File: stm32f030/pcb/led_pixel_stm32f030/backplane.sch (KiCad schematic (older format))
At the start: 3 parts, among them J1 Screw_Terminal_1x02, J2 CONN_01X10, J3 CONN_01X10

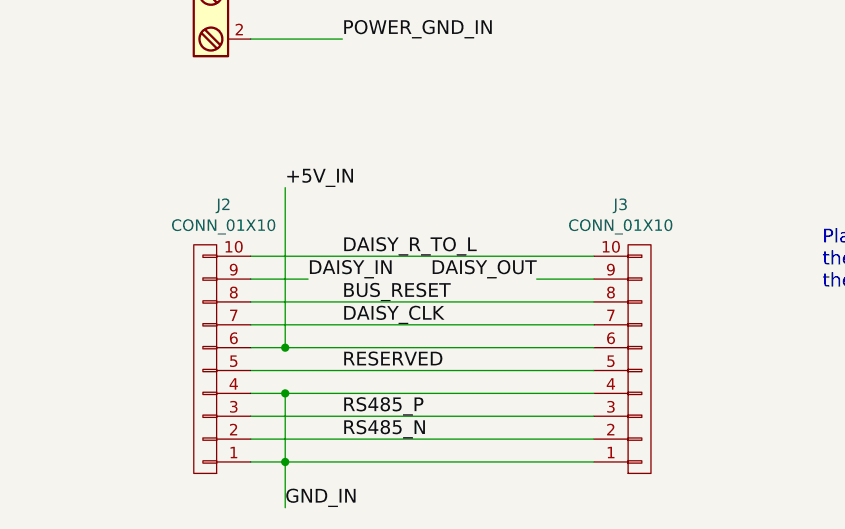
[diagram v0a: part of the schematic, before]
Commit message: made a first layout draft...
well okay, wouldn´t call it layout yet ;)

- next step make it look like a Layout XD
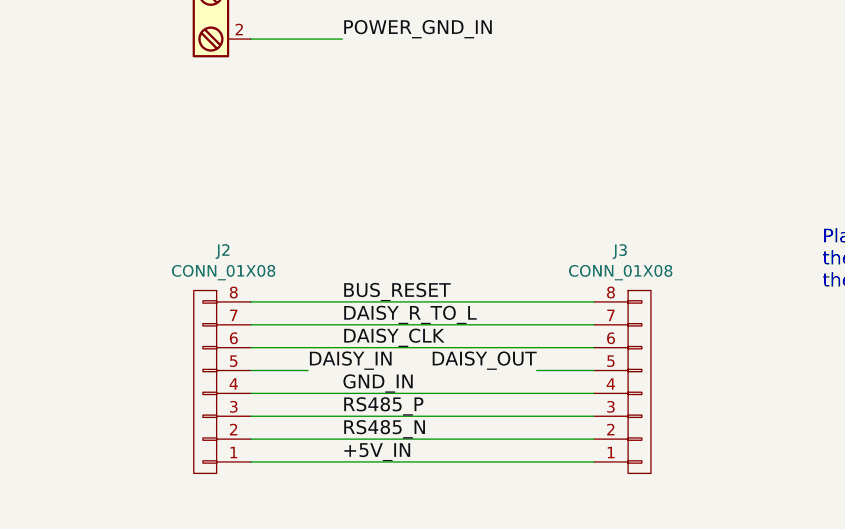
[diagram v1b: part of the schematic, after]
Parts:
- removed J2, J3: CONN_01X10, Pin_Headers:Pin_Header_Straight_1x10_Pitch2.54mm, symbol CONN_01X10
- added J2, J3: CONN_01X08, Pin_Headers:Pin_Header_Straight_1x08_Pitch2.54mm, symbol CONN_01X08
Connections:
- net +5V_IN: now also J2.1 (P1), J3.1 (P1)
- net BUS_RESET: now also J2.8 (P8), J3.8 (P8)
- net DAISY_CLK: now also J2.6 (P6), J3.6 (P6)
- net DAISY_IN: now also J2.5 (P5)
- net DAISY_OUT: now also J3.5 (P5)
- net DAISY_R_TO_L: now also J2.7 (P7), J3.7 (P7)
- net GND_IN: now also J2.4 (P4), J3.4 (P4)
- net RS485_N: now also J2.2 (P2), J3.2 (P2)
- net RS485_P: now also J2.3 (P3), J3.3 (P3)
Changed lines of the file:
@@
 $EndDescr
-$Comp
-L CONN_01X10 J2
-U 1 1 5905FA3B
-P 3400 3350
-F 0 "J2" H 3319 2675 50  0000 C CNN
-F 1 "CONN_01X10" H 3319 2766 50  0000 C CNN
-F 2 "Pin_Headers:Pin_Header_Straight_1x10_Pitch2.54mm" H 3400 3350 50  0001 C CNN
-F 3 "" H 3400 3350 50  0001 C CNN
-	1    3400 3350
-	-1   0    0    1
-$EndComp
-$Comp
-L CONN_01X10 J3
-U 1 1 5905FABB
-P 5300 3350
-F 0 "J3" H 5218 2675 50  0000 C CNN
-F 1 "CONN_01X10" H 5218 2766 50  0000 C CNN
-F 2 "Pin_Headers:Pin_Header_Straight_1x10_Pitch2.54mm" H 5300 3350 50  0001 C CNN
-F 3 "" H 5300 3350 50  0001 C CNN
-	1    5300 3350
-	1    0    0    1
-$EndComp
 $Comp
 L Screw_Terminal_1x02 J1
@@
 	1    0    0    -1
 $EndComp
-Wire Wire Line
-	3600 1750 4000 1750
-Wire Wire Line
-	3600 1950 4000 1950
-Wire Wire Line
-	3600 2900 5100 2900
-Wire Wire Line
-	3600 3500 5100 3500
-Wire Wire Line
-	3600 3800 5100 3800
-Wire Wire Line
-	3600 3700 5100 3700
-Wire Wire Line
-	5100 3600 3600 3600
-Wire Wire Line
-	3750 3500 3750 4000
-Connection ~ 3750 3800
-Connection ~ 3750 3500
 Text Label 4000 3600 0    60   ~ 0
 RS485_P
 Text Label 4000 3700 0    60   ~ 0
 RS485_N
-Text Label 4000 2900 0    60   ~ 0
+Text Label 4000 3200 0    60   ~ 0
 DAISY_R_TO_L
-Text Label 3850 3000 0    60   ~ 0
+Text Label 3850 3400 0    60   ~ 0
 DAISY_IN
-Text Label 4850 3000 2    60   ~ 0
+Text Label 4850 3400 2    60   ~ 0
 DAISY_OUT
-Wire Wire Line
-	5100 3000 4850 3000
-Wire Wire Line
-	3850 3000 3600 3000
-Wire Wire Line
-	5100 3100 3600 3100
 Text Label 4000 3100 0    60   ~ 0
 BUS_RESET
-Text Label 4000 3200 0    60   ~ 0
+Text Label 4000 3300 0    60   ~ 0
 DAISY_CLK
-Wire Wire Line
-	3600 3200 5100 3200
-Wire Wire Line
-	3600 3300 5100 3300
-Wire Wire Line
-	5100 3400 3600 3400
-Wire Wire Line
-	3750 2600 3750 3300
-Connection ~ 3750 3300
-Text Label 4000 3400 0    60   ~ 0
-RESERVED
 Text Notes 6100 3050 0    60   ~ 0
 Place both pin headers on the same height\nthey have to be 1,27mm away from the edge of the pcb\nthe connections between 2 pcbs is done using standard 2,54mm jumpers
@@
 Text HLabel 1250 2550 0    60   Output ~ 0
 GND_IN
-Text Label 3750 4000 0    60   ~ 0
+Text Label 4000 3500 0    60   ~ 0
 GND_IN
-Text Label 3750 2600 0    60   ~ 0
+Text Label 4000 3800 0    60   ~ 0
 +5V_IN
 Text Label 4000 1750 0    60   ~ 0
@@
 Text Label 1400 1850 0    60   ~ 0
 DAISY_CLK
+$Comp
+L CONN_01X08 J2
+U 1 1 59073CA8
+P 3400 3450
+F 0 "J2" H 3319 2875 50  0000 C CNN
+F 1 "CONN_01X08" H 3319 2966 50  0000 C CNN
+F 2 "Pin_Headers:Pin_Header_Straight_1x08_Pitch2.54mm" H 3400 3450 50  0001 C CNN
+F 3 "" H 3400 3450 50  0001 C CNN
+	1    3400 3450
+	-1   0    0    1
+$EndComp
+$Comp
+L CONN_01X08 J3
+U 1 1 59073D32
+P 5300 3450
+F 0 "J3" H 5218 2875 50  0000 C CNN
+F 1 "CONN_01X08" H 5218 2966 50  0000 C CNN
+F 2 "Pin_Headers:Pin_Header_Straight_1x08_Pitch2.54mm" H 5300 3450 50  0001 C CNN
+F 3 "" H 5300 3450 50  0001 C CNN
+	1    5300 3450
+	1    0    0    1
+$EndComp
+Wire Wire Line
+	3600 1750 4000 1750
+Wire Wire Line
+	3600 1950 4000 1950
+Wire Wire Line
+	3600 3500 5100 3500
+Wire Wire Line
+	3600 3800 5100 3800
+Wire Wire Line
+	3600 3700 5100 3700
+Wire Wire Line
+	5100 3600 3600 3600
+Wire Wire Line
+	5100 3100 3600 3100
+Wire Wire Line
+	3600 3200 5100 3200
 Wire Wire Line
 	1400 1050 1250 1050
@@
 Wire Wire Line
 	1400 2550 1250 2550
+Wire Wire Line
+	3850 3400 3600 3400
+Wire Wire Line
+	4850 3400 5100 3400
+Wire Wire Line
+	3600 3300 5100 3300
 $EndSCHEMATC
